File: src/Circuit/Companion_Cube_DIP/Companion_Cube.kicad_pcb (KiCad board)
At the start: 2 copper layers, 43.2 x 43.2 mm, 21 parts, among them CON1 AVR-ISP-6, IC1 ATTINY85-S, P1 LED_4, P2 LED_3, P3 LED_2, P4 LED_1, P5 CONN_1, P6 CONN_1, P7 CONN_1, U1 MINI-B_USB

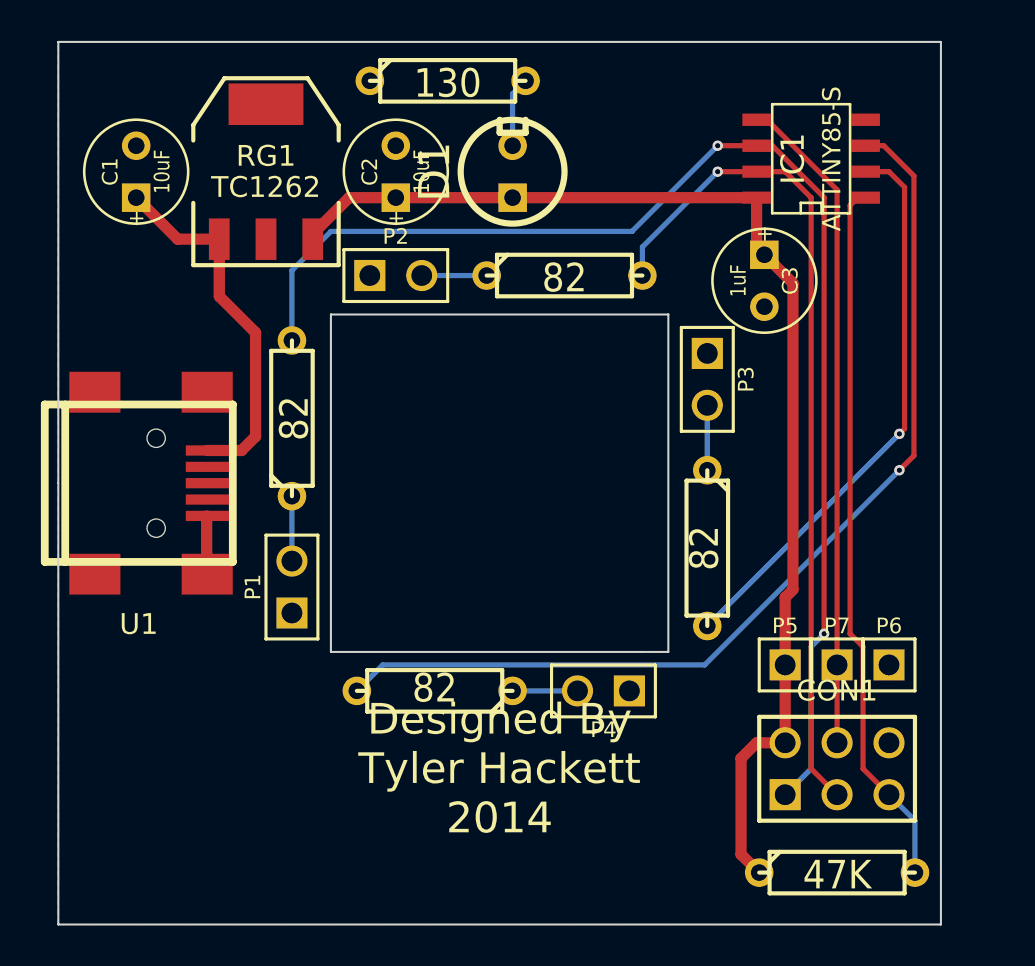
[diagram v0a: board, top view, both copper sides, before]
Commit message: Added attiny85 DIP version
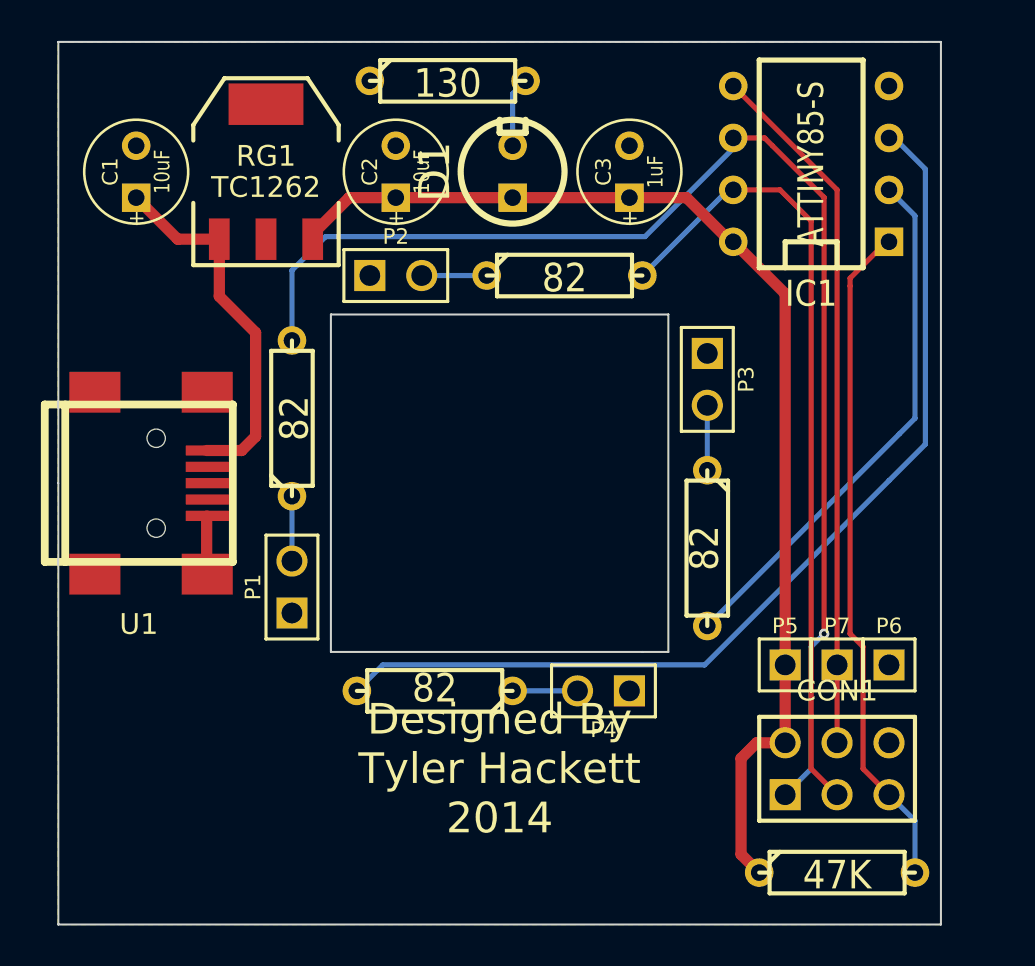
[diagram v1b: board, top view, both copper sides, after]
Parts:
- IC1: footprint SO8E -> DIP-8__300
- moved C3 8.49 mm to (205.7, 115.6), turned to 90 degrees
- moved IC1 0.25 mm to (214.6, 115.2)
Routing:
- net VCC: track 58.7 -> 56.5 mm
- net N-000006: track 41.4 -> 39.3 mm, vias 1 -> 0
- net N-000002: track 34.9 -> 33.0 mm
- net N-000003: track 32.4 -> 34.2 mm
- net N-000005: track 27.7 -> 26.1 mm, vias 1 -> 0
- net N-000007: track 63.0 -> 63.9 mm, vias 2 -> 1
- net N-000004: vias 1 -> 0

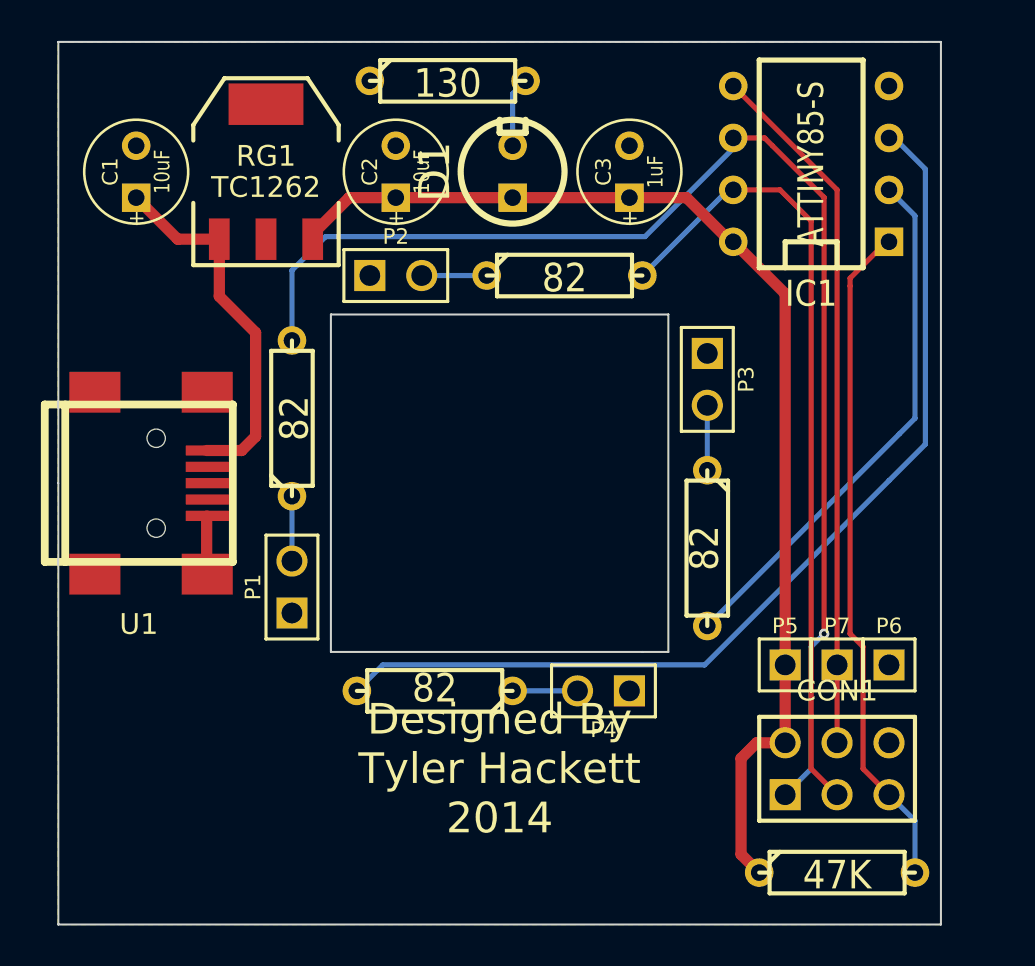
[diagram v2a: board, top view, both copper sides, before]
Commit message: Widened hole on cube circuit, smaller button PCB
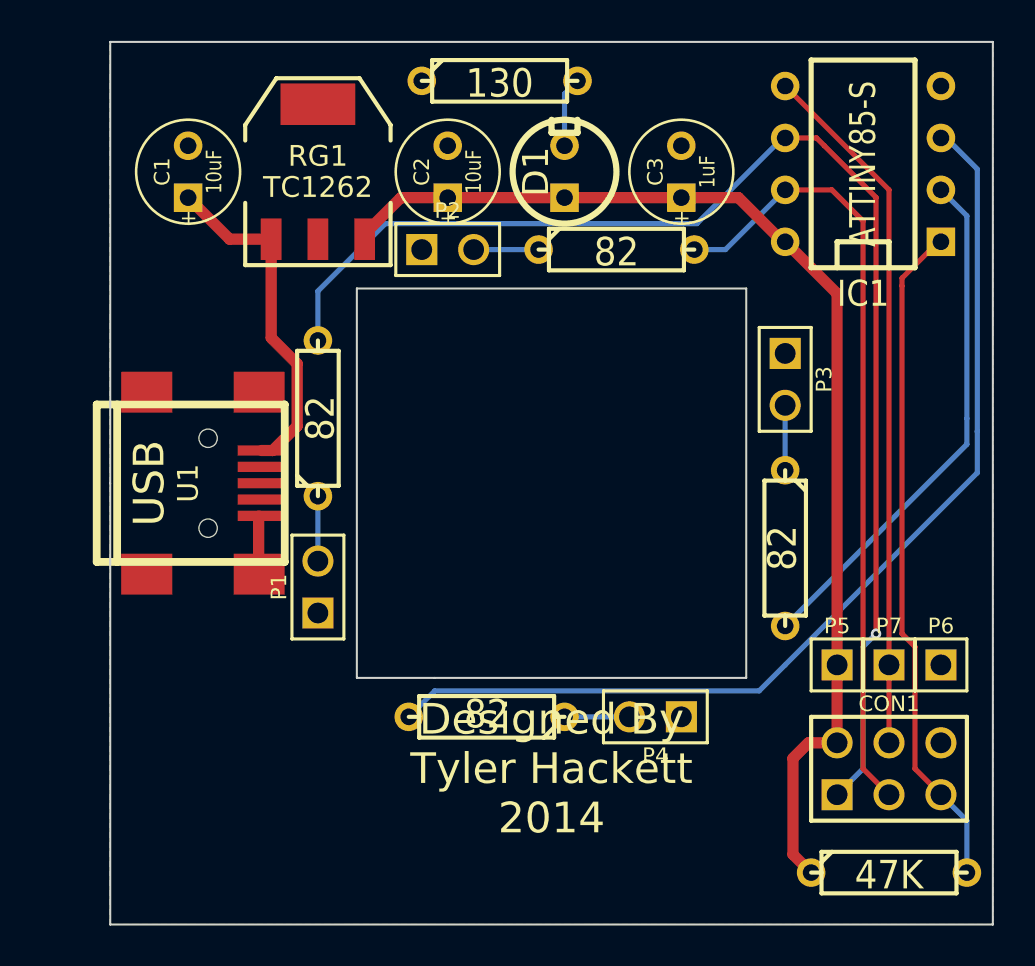
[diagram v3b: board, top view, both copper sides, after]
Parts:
- moved P3 3.81 mm to (213.4, 125.7)
- moved R3 3.81 mm to (213.4, 134.0)
- moved P2 2.84 mm to (196.8, 119.4)
- moved P4 2.84 mm to (207.0, 142.2)
- moved R2 2.84 mm to (205.1, 119.4)
- moved R4 2.84 mm to (198.8, 142.2)
- moved C1 2.54 mm to (184.2, 115.6)
- moved C2 2.54 mm to (196.8, 115.6)
- moved C3 2.54 mm to (208.3, 115.6)
- moved CON1 2.54 mm to (218.4, 144.8)
- moved D1 2.54 mm to (202.6, 115.6)
- moved IC1 2.54 mm to (217.2, 115.2)
- moved P5 2.54 mm to (215.9, 139.7)
- moved P6 2.54 mm to (221.0, 139.7)
- moved P7 2.54 mm to (218.4, 139.7)
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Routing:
- net N-000004: track 48.7 -> 50.0 mm
- net N-0000017: track 18.0 -> 16.8 mm
- net N-000006: track 39.3 -> 38.7 mm
- net N-000005: track 26.1 -> 25.5 mm
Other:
- outline, holes or cut-outs redrawn
- board text added: "CUT OUT"
- board text added: "USB"

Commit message: Cleaned up wiring to attiny on PCB
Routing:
- net N-000006: track 38.7 -> 37.4 mm
- net N-000007: track 64.0 -> 63.1 mm
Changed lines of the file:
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@@
     (thickness 1.6)
     (drawings 14)
-    (tracks 73)
+    (tracks 69)
     (zones 0)
     (modules 21)
@@
   (segment (start 188.214 118.872) (end 186.182 118.872) (width 0.55) (layer F.Cu) (net 5))
   (segment (start 186.182 118.872) (end 184.15 116.84) (width 0.55) (layer F.Cu) (net 5))
-  (segment (start 220.98 118.999) (end 220.853 118.999) (width 0.254) (layer F.Cu) (net 6))
-  (segment (start 219.075 120.777) (end 219.075 121.158) (width 0.254) (layer F.Cu) (net 6))
-  (segment (start 220.853 118.999) (end 219.075 120.777) (width 0.254) (layer F.Cu) (net 6))
+  (segment (start 220.98 118.999) (end 219.075 120.904) (width 0.254) (layer F.Cu) (net 6) (status 400000))
+  (segment (start 219.075 120.904) (end 219.075 121.285) (width 0.254) (layer F.Cu) (net 6))
   (segment (start 220.98 146.05) (end 219.71 144.78) (width 0.254) (layer F.Cu) (net 6))
   (segment (start 219.71 144.78) (end 219.71 138.811) (width 0.254) (layer F.Cu) (net 6))
   (segment (start 219.71 138.811) (end 219.075 138.176) (width 0.254) (layer F.Cu) (net 6))
-  (segment (start 219.075 138.176) (end 219.075 121.158) (width 0.254) (layer F.Cu) (net 6))
+  (segment (start 219.075 138.176) (end 219.075 121.285) (width 0.254) (layer F.Cu) (net 6))
   (segment (start 222.25 149.86) (end 222.25 147.32) (width 0.254) (layer B.Cu) (net 6))
   (segment (start 222.25 147.32) (end 220.98 146.05) (width 0.254) (layer B.Cu) (net 6))
@@
   (segment (start 220.98 116.459) (end 222.25 117.729) (width 0.254) (layer B.Cu) (net 9))
   (segment (start 222.25 117.729) (end 222.25 127.635) (width 0.254) (layer B.Cu) (net 9))
+  (segment (start 213.36 116.459) (end 217.17 120.269) (width 0.254) (layer F.Cu) (net 10))
   (segment (start 208.915 119.38) (end 210.439 119.38) (width 0.254) (layer B.Cu) (net 10))
   (segment (start 210.439 119.38) (end 213.36 116.459) (width 0.254) (layer B.Cu) (net 10))
-  (segment (start 213.36 116.459) (end 215.646 116.459) (width 0.254) (layer F.Cu) (net 10))
-  (segment (start 215.646 116.459) (end 217.17 117.983) (width 0.254) (layer F.Cu) (net 10))
   (segment (start 217.17 144.78) (end 218.44 146.05) (width 0.254) (layer F.Cu) (net 10))
-  (segment (start 217.17 117.983) (end 217.17 144.78) (width 0.254) (layer F.Cu) (net 10))
+  (segment (start 217.17 120.269) (end 217.17 144.78) (width 0.254) (layer F.Cu) (net 10))
+  (segment (start 213.36 113.919) (end 217.805 118.364) (width 0.254) (layer F.Cu) (net 11))
   (segment (start 213.36 113.919) (end 213.233 113.919) (width 0.254) (layer B.Cu) (net 11))
   (segment (start 190.5 121.412) (end 190.5 123.825) (width 0.254) (layer B.Cu) (net 11))
@@
   (segment (start 209.042 118.11) (end 193.802 118.11) (width 0.254) (layer B.Cu) (net 11))
   (segment (start 213.233 113.919) (end 209.042 118.11) (width 0.254) (layer B.Cu) (net 11))
-  (segment (start 213.36 113.919) (end 214.895582 113.919) (width 0.254) (layer F.Cu) (net 11))
-  (segment (start 214.895582 113.919) (end 215.276582 114.3) (width 0.254) (layer F.Cu) (net 11))
   (segment (start 217.17 144.78) (end 215.9 146.05) (width 0.254) (layer B.Cu) (net 11))
   (segment (start 217.17 138.811) (end 217.17 144.78) (width 0.254) (layer B.Cu) (net 11))
   (segment (start 217.805 138.176) (end 217.17 138.811) (width 0.254) (layer B.Cu) (net 11))
   (via (at 217.805 138.176) (size 0.508) (layers F.Cu B.Cu) (net 11))
-  (segment (start 217.805 116.828418) (end 217.805 138.176) (width 0.254) (layer F.Cu) (net 11))
-  (segment (start 215.276582 114.3) (end 217.805 116.828418) (width 0.254) (layer F.Cu) (net 11))
+  (segment (start 217.805 118.364) (end 217.805 138.176) (width 0.254) (layer F.Cu) (net 11))
   (segment (start 202.565 142.24) (end 205.74 142.24) (width 0.254) (layer B.Cu) (net 12))
   (segment (start 202.565 114.3) (end 202.565 111.76) (width 0.254) (layer B.Cu) (net 13))
